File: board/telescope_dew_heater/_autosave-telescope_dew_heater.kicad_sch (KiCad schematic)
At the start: 39 parts, among them J1 RCA1, J2 RCA1, J3 RCA1, J4 RCA1, J5 Barrel_Jack, Q1 Q_NMOS_GDS, Q2 Q_NMOS_GDS, Q3 Q_NMOS_GDS, Q4 Q_NMOS_GDS, SW1 SW_DPDT_x2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

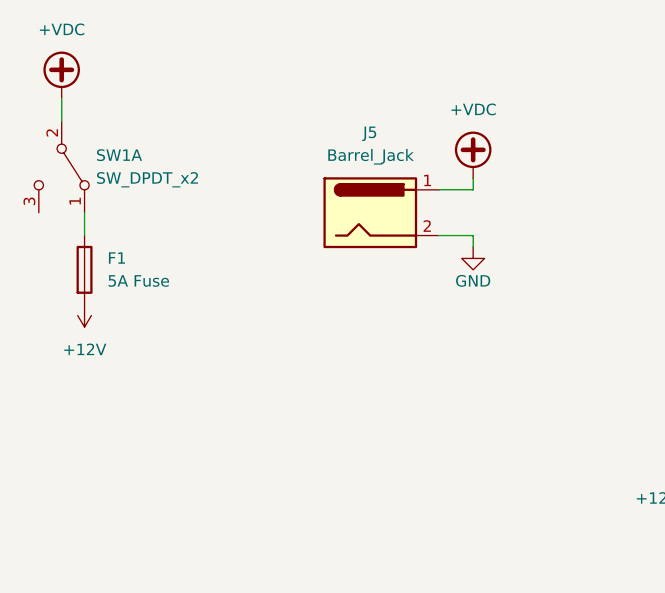
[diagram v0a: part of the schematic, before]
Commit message: 4 channel version
4 channel version of design. Committing in case I need to roll back
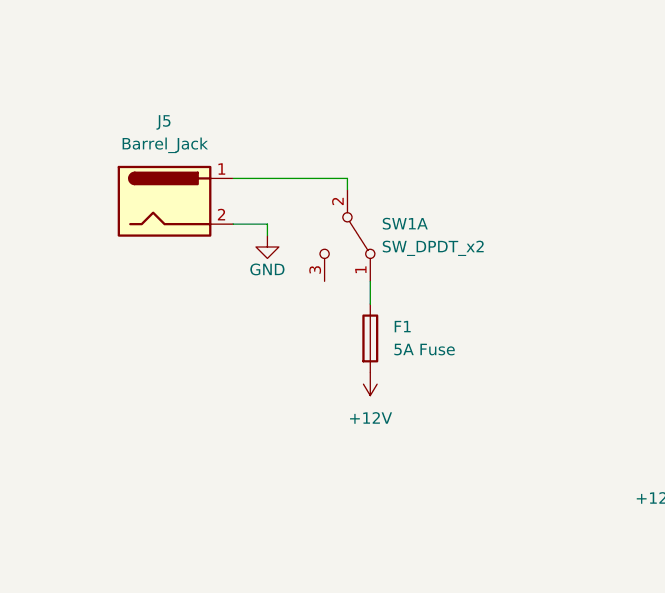
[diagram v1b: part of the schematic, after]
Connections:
- net +VDC: no longer names the net of J5.1, SW1.2 (B)
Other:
- moved on the sheet: F1, J5, SW1A
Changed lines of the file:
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@@
     (stroke (width 0) (type default))
   )
-  (wire (pts (xy 64.77 36.83) (xy 60.96 36.83))
+  (wire (pts (xy 41.91 35.56) (xy 38.1 35.56))
     (stroke (width 0) (type default))
   )
@@
     (stroke (width 0) (type default))
   )
+  (wire (pts (xy 38.1 30.48) (xy 50.8 30.48))
+    (stroke (width 0) (type default))
+  )
   (wire (pts (xy 121.92 60.96) (xy 127 60.96))
     (stroke (width 0) (type default))
@@
     (stroke (width 0) (type default))
   )
-  (wire (pts (xy 60.96 31.75) (xy 64.77 31.75))
-    (stroke (width 0) (type default))
-  )
   (wire (pts (xy 227.33 142.24) (xy 231.14 142.24))
     (stroke (width 0) (type default))
   )
+  (wire (pts (xy 50.8 30.48) (xy 50.8 31.75))
+    (stroke (width 0) (type default))
+  )
   (wire (pts (xy 204.47 114.3) (xy 204.47 113.03))
     (stroke (width 0) (type default))
@@
     (stroke (width 0) (type default))
   )
-  (wire (pts (xy 64.77 38.1) (xy 64.77 36.83))
+  (wire (pts (xy 41.91 36.83) (xy 41.91 35.56))
     (stroke (width 0) (type default))
   )
@@
     (stroke (width 0) (type default))
   )
-  (wire (pts (xy 21.59 34.29) (xy 21.59 36.83))
+  (wire (pts (xy 53.34 41.91) (xy 53.34 44.45))
     (stroke (width 0) (type default))
   )
@@
     (stroke (width 0) (type default))
   )
-  (wire (pts (xy 64.77 31.75) (xy 64.77 30.48))
-    (stroke (width 0) (type default))
-  )
   (wire (pts (xy 234.95 58.42) (xy 234.95 57.15))
     (stroke (width 0) (type default))
@@
     (stroke (width 0) (type default))
   )
-  (wire (pts (xy 19.05 21.59) (xy 19.05 24.13))
-    (stroke (width 0) (type default))
-  )
   (wire (pts (xy 213.36 36.83) (xy 213.36 40.64))
     (stroke (width 0) (type default))
@@
         (path "/7623b60a-e6f6-4f34-9d33-2b09fb9bf88f"
           (reference "Q3") (unit 1)
-        )
-      )
-    )
-  )
-  (symbol (lib_id "power:+VDC") (at 64.77 30.48 0) (unit 1)
-    (in_bom yes) (on_board yes) (dnp no) (fields_autoplaced)
-    (property "Reference" "#PWR031" (at 64.77 33.02 0)
-      (effects (font (size 1.27 1.27)) hide)
-    )
-    (property "Value" "+VDC" (at 64.77 22.86 0)
-      (effects (font (size 1.27 1.27)))
-    )
-    (property "Footprint" "" (at 64.77 30.48 0)
-      (effects (font (size 1.27 1.27)) hide)
-    )
-    (property "Datasheet" "" (at 64.77 30.48 0)
-      (effects (font (size 1.27 1.27)) hide)
-    )
-    (pin "1")
-    (instances
-      (project "telescope_dew_heater"
-        (path "/7623b60a-e6f6-4f34-9d33-2b09fb9bf88f"
-          (reference "#PWR031") (unit 1)
         )
       )
@@
     )
   )
-  (symbol (lib_id "power:+12V") (at 21.59 44.45 180) (unit 1)
-    (in_bom yes) (on_board yes) (dnp no) (fields_autoplaced)
-    (property "Reference" "#PWR010" (at 21.59 40.64 0)
-      (effects (font (size 1.27 1.27)) hide)
-    )
-    (property "Value" "+12V" (at 21.59 49.53 0)
-      (effects (font (size 1.27 1.27)))
-    )
-    (property "Footprint" "" (at 21.59 44.45 0)
-      (effects (font (size 1.27 1.27)) hide)
-    )
-    (property "Datasheet" "" (at 21.59 44.45 0)
+  (symbol (lib_id "power:+12V") (at 53.34 52.07 180) (unit 1)
+    (in_bom yes) (on_board yes) (dnp no) (fields_autoplaced)
+    (property "Reference" "#PWR010" (at 53.34 48.26 0)
+      (effects (font (size 1.27 1.27)) hide)
+    )
+    (property "Value" "+12V" (at 53.34 57.15 0)
+      (effects (font (size 1.27 1.27)))
+    )
+    (property "Footprint" "" (at 53.34 52.07 0)
+      (effects (font (size 1.27 1.27)) hide)
+    )
+    (property "Datasheet" "" (at 53.34 52.07 0)
       (effects (font (size 1.27 1.27)) hide)
     )
@@
     )
   )
-  (symbol (lib_id "Device:Fuse") (at 21.59 40.64 0) (unit 1)
-    (in_bom yes) (on_board yes) (dnp no) (fields_autoplaced)
-    (property "Reference" "F1" (at 24.13 39.37 0)
-      (effects (font (size 1.27 1.27)) (justify left))
-    )
-    (property "Value" "5A Fuse" (at 24.13 41.91 0)
-      (effects (font (size 1.27 1.27)) (justify left))
-    )
-    (property "Footprint" "My Footprints:Fuseholder_Cylinder-5x20mm_Wuerth_696108003002_THT" (at 19.812 40.64 90)
-      (effects (font (size 1.27 1.27)) hide)
-    )
-    (property "Datasheet" "~" (at 21.59 40.64 0)
+  (symbol (lib_id "Device:Fuse") (at 53.34 48.26 0) (unit 1)
+    (in_bom yes) (on_board yes) (dnp no) (fields_autoplaced)
+    (property "Reference" "F1" (at 55.88 46.99 0)
+      (effects (font (size 1.27 1.27)) (justify left))
+    )
+    (property "Value" "5A Fuse" (at 55.88 49.53 0)
+      (effects (font (size 1.27 1.27)) (justify left))
+    )
+    (property "Footprint" "My Footprints:Fuseholder_Cylinder-5x20mm_Wuerth_696108003002_THT" (at 51.562 48.26 90)
+      (effects (font (size 1.27 1.27)) hide)
+    )
+    (property "Datasheet" "~" (at 53.34 48.26 0)
       (effects (font (size 1.27 1.27)) hide)
     )
@@
     )
   )
-  (symbol (lib_id "Connector:Barrel_Jack") (at 53.34 34.29 0) (unit 1)
-    (in_bom yes) (on_board yes) (dnp no) (fields_autoplaced)
-    (property "Reference" "J5" (at 53.34 25.4 0)
-      (effects (font (size 1.27 1.27)))
-    )
-    (property "Value" "Barrel_Jack" (at 53.34 27.94 0)
-      (effects (font (size 1.27 1.27)))
-    )
-    (property "Footprint" "Connector_BarrelJack:BarrelJack_CUI_PJ-063AH_Horizontal" (at 54.61 35.306 0)
-      (effects (font (size 1.27 1.27)) hide)
-    )
-    (property "Datasheet" "~" (at 54.61 35.306 0)
+  (symbol (lib_id "Connector:Barrel_Jack") (at 30.48 33.02 0) (unit 1)
+    (in_bom yes) (on_board yes) (dnp no) (fields_autoplaced)
+    (property "Reference" "J5" (at 30.48 24.13 0)
+      (effects (font (size 1.27 1.27)))
+    )
+    (property "Value" "Barrel_Jack" (at 30.48 26.67 0)
+      (effects (font (size 1.27 1.27)))
+    )
+    (property "Footprint" "Connector_BarrelJack:BarrelJack_CUI_PJ-063AH_Horizontal" (at 31.75 34.036 0)
+      (effects (font (size 1.27 1.27)) hide)
+    )
+    (property "Datasheet" "~" (at 31.75 34.036 0)
       (effects (font (size 1.27 1.27)) hide)
     )
@@
     )
   )
-  (symbol (lib_id "power:GND") (at 64.77 38.1 0) (unit 1)
+  (symbol (lib_id "power:GND") (at 41.91 36.83 0) (unit 1)
     (in_bom yes) (on_board yes) (dnp no)
-    (property "Reference" "#PWR032" (at 64.77 44.45 0)
-      (effects (font (size 1.27 1.27)) hide)
-    )
-    (property "Value" "GND" (at 64.77 41.91 0)
-      (effects (font (size 1.27 1.27)))
-    )
-    (property "Footprint" "" (at 64.77 38.1 0)
-      (effects (font (size 1.27 1.27)) hide)
-    )
-    (property "Datasheet" "" (at 64.77 38.1 0)
+    (property "Reference" "#PWR032" (at 41.91 43.18 0)
+      (effects (font (size 1.27 1.27)) hide)
+    )
+    (property "Value" "GND" (at 41.91 40.64 0)
+      (effects (font (size 1.27 1.27)))
+    )
+    (property "Footprint" "" (at 41.91 36.83 0)
+      (effects (font (size 1.27 1.27)) hide)
+    )
+    (property "Datasheet" "" (at 41.91 36.83 0)
       (effects (font (size 1.27 1.27)) hide)
     )
@@
     )
   )
-  (symbol (lib_id "power:+VDC") (at 19.05 21.59 0) (unit 1)
-    (in_bom yes) (on_board yes) (dnp no) (fields_autoplaced)
-    (property "Reference" "#PWR01" (at 19.05 24.13 0)
-      (effects (font (size 1.27 1.27)) hide)
-    )
-    (property "Value" "+VDC" (at 19.05 13.97 0)
-      (effects (font (size 1.27 1.27)))
-    )
-    (property "Footprint" "" (at 19.05 21.59 0)
-      (effects (font (size 1.27 1.27)) hide)
-    )
-    (property "Datasheet" "" (at 19.05 21.59 0)
-      (effects (font (size 1.27 1.27)) hide)
-    )
-    (pin "1")
-    (instances
-      (project "telescope_dew_heater"
-        (path "/7623b60a-e6f6-4f34-9d33-2b09fb9bf88f"
-          (reference "#PWR01") (unit 1)
-        )
-      )
-    )
-  )
   (symbol (lib_id "power:+12V") (at 214.63 109.22 0) (unit 1)
     (in_bom yes) (on_board yes) (dnp no) (fields_autoplaced)
@@
     )
   )
-  (symbol (lib_id "Switch:SW_DPDT_x2") (at 19.05 29.21 270) (unit 1)
-    (in_bom yes) (on_board yes) (dnp no) (fields_autoplaced)
-    (property "Reference" "SW1" (at 22.86 27.94 90)
-      (effects (font (size 1.27 1.27)) (justify left))
-    )
-    (property "Value" "SW_DPDT_x2" (at 22.86 30.48 90)
-      (effects (font (size 1.27 1.27)) (justify left))
-    )
-    (property "Footprint" "Connector_PinHeader_2.54mm:PinHeader_1x02_P2.54mm_Vertical" (at 19.05 29.21 0)
-      (effects (font (size 1.27 1.27)) hide)
-    )
-    (property "Datasheet" "~" (at 19.05 29.21 0)
-      (effects (font (size 1.27 1.27)) hide)
-    )
+  (symbol (lib_id "Switch:SW_DPDT_x2") (at 50.8 36.83 270) (unit 1)
+    (in_bom yes) (on_board yes) (dnp no) (fields_autoplaced)
+    (property "Reference" "SW1" (at 54.61 35.56 90)
+      (effects (font (size 1.27 1.27)) (justify left))
+    )
+    (property "Value" "SW_DPDT_x2" (at 54.61 38.1 90)
+      (effects (font (size 1.27 1.27)) (justify left))
+    )
+    (property "Footprint" "Connector_PinHeader_2.54mm:PinHeader_1x02_P2.54mm_Vertical" (at 50.8 36.83 0)
+      (effects (font (size 1.27 1.27)) hide)
+    )
+    (property "Datasheet" "~" (at 50.8 36.83 0)
+      (effects (font (size 1.27 1.27)) hide)
+    )
